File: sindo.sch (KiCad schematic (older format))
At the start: 145 parts

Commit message: Finished lables, might still need pull-downs
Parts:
- removed U?: ESP32-DEVKITC-32D, MODULE_ESP32-DEVKITC-32D, symbol ESP32-DEVKITC-32D:ESP32-DEVKITC-32D
- added J? (x2): Conn_2Rows-13Pins, symbol Connector_Generic:Conn_2Rows-13Pins
- added U?: ESP32DEVKITV1, ESP32-DEVKITV1, symbol ESP32DEVKITV1:ESP32DEVKITV1
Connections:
- net labels added: C10, C11, C6, C7, C8, C9, COL0, COL1, COL10, COL11, COL2, COL3, COL4, COL5, COL6, COL7, COL8, COL9, R0, R1, R2, R3, R4, R5, ROW0, ROW1, ROW2, ROW3, ROW4, ROW5
- wire segments 432 -> 474

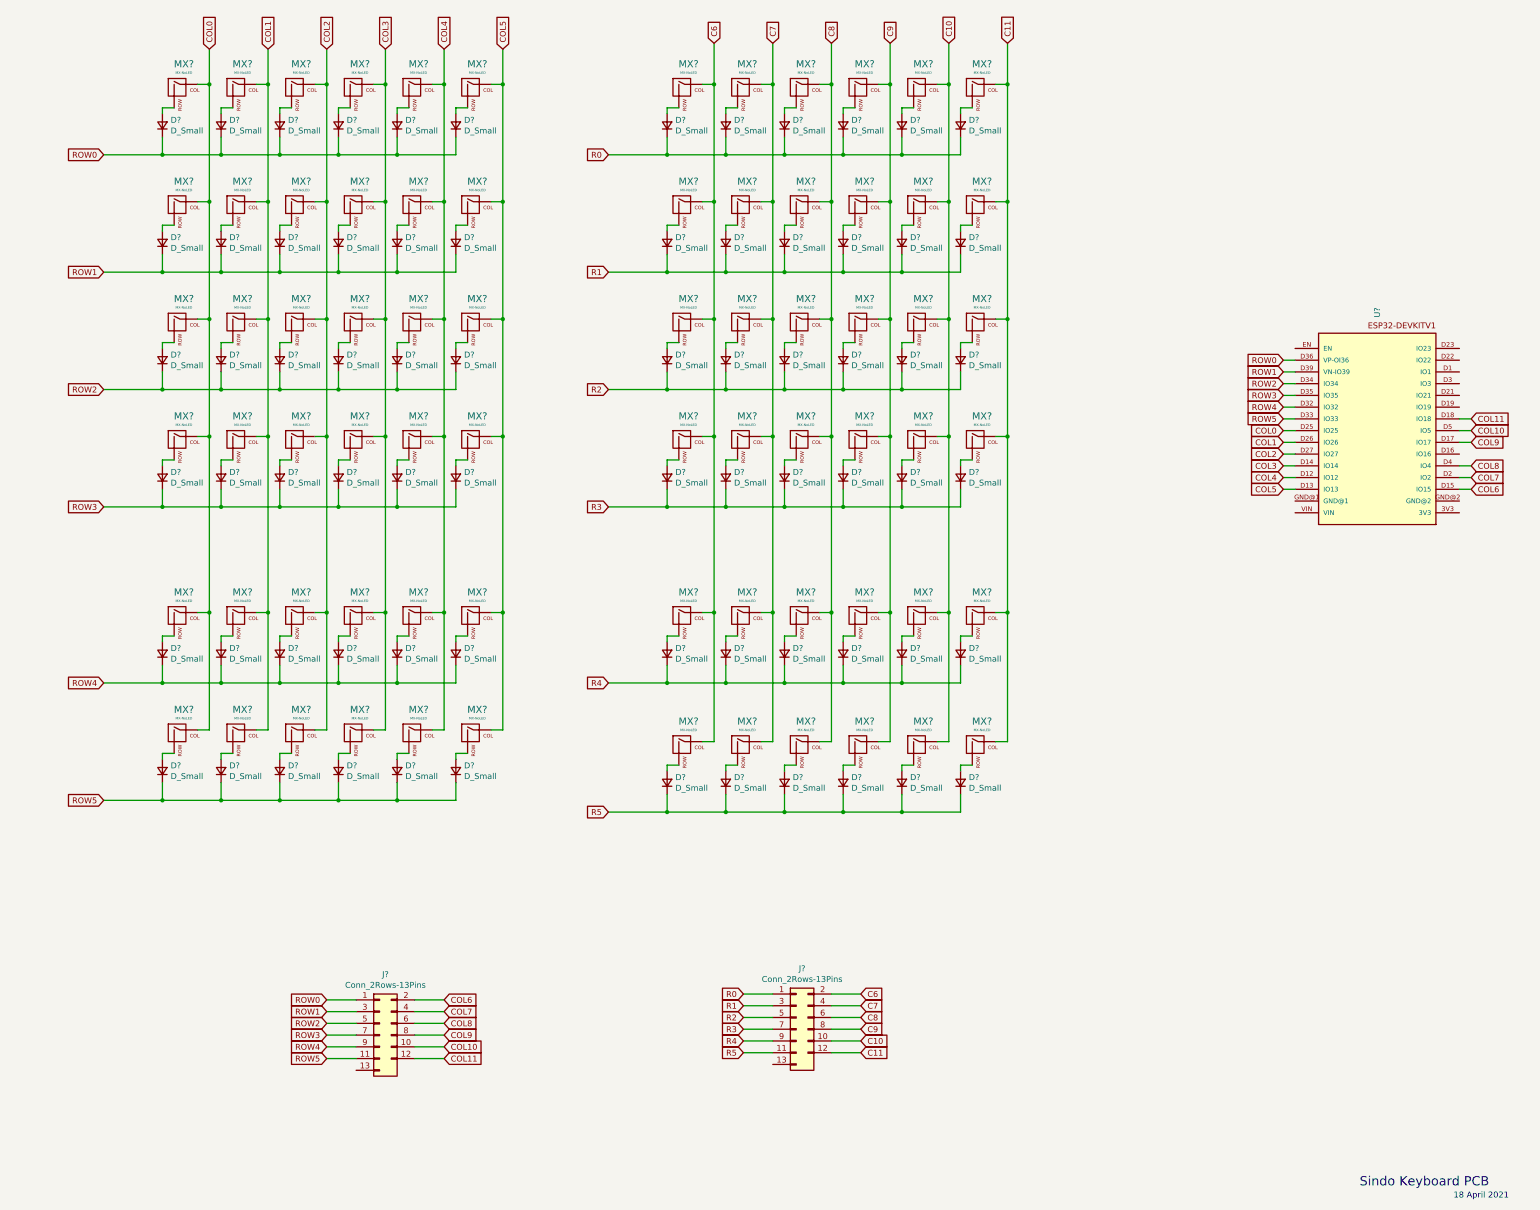
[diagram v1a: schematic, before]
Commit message: Added pull down resistors to rows
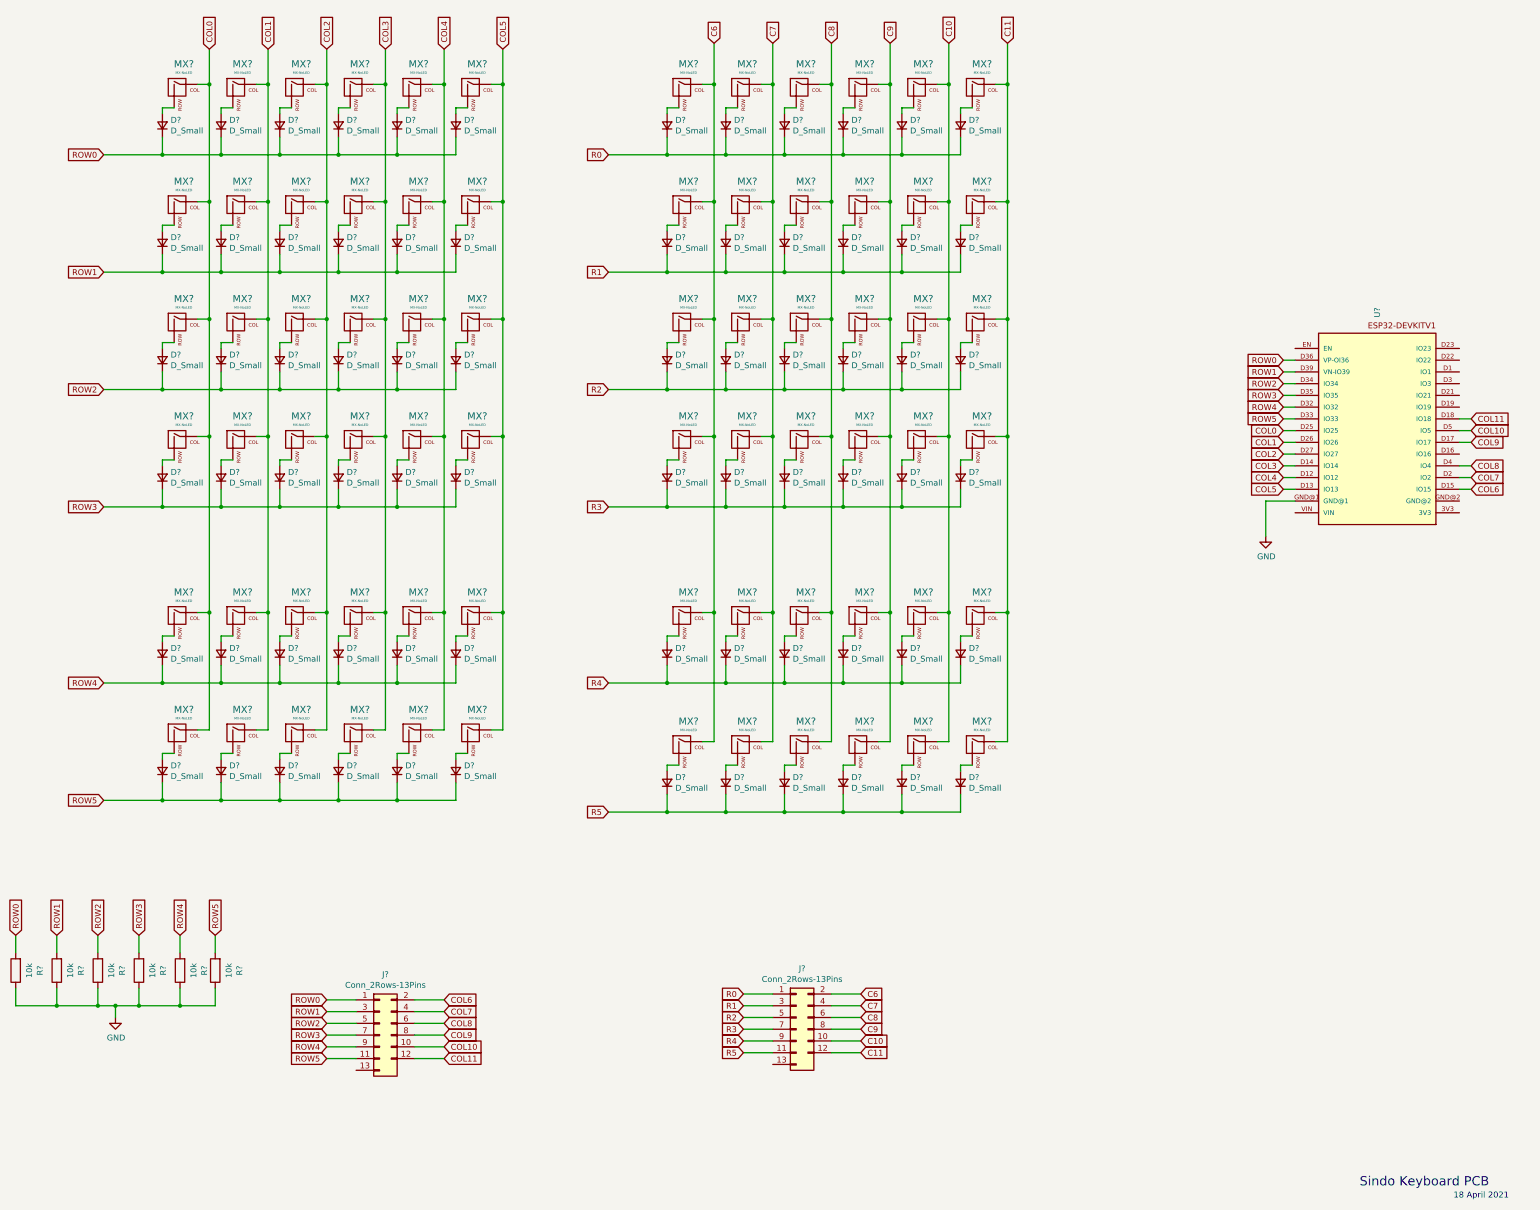
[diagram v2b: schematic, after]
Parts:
- added R? (x6): 10k, symbol Device:R
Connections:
- net ROW0: now also R?.2
- net ROW1: now also R?.2
- net ROW2: now also R?.2
- net ROW3: now also R?.2
- net ROW4: now also R?.2
- net ROW5: now also R?.2
- net GND: now reaches U?.GND@1
- net GND: now also R?.1, R?.1, R?.1, R?.1, R?.1, R?.1
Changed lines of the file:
@@
 Wire Wire Line
 	7950 9300 7700 9300
+Text GLabel 750  8800 1    50   Input ~ 0
+ROW0
+Text GLabel 1100 8800 1    50   Input ~ 0
+ROW1
+Text GLabel 1450 8800 1    50   Input ~ 0
+ROW2
+Text GLabel 1800 8800 1    50   Input ~ 0
+ROW3
+Text GLabel 2150 8800 1    50   Input ~ 0
+ROW4
+Text GLabel 2450 8800 1    50   Input ~ 0
+ROW5
+$Comp
+L power:GND #PWR?
+U 1 1 6084C65C
+P 1600 9500
+F 0 "#PWR?" H 1600 9250 50  0001 C CNN
+F 1 "GND" H 1605 9327 50  0000 C CNN
+F 2 "" H 1600 9500 50  0001 C CNN
+F 3 "" H 1600 9500 50  0001 C CNN
+	1    1600 9500
+	1    0    0    -1
+$EndComp
+$Comp
+L Device:R R?
+U 1 1 60854EEB
+P 750 9100
+F 0 "R?" V 543 9100 50  0000 C CNN
+F 1 "10k" V 634 9100 50  0000 C CNN
+F 2 "" V 680 9100 50  0001 C CNN
+F 3 "~" H 750 9100 50  0001 C CNN
+	1    750  9100
+	-1   0    0    1
+$EndComp
+$Comp
+L Device:R R?
+U 1 1 60856611
+P 1100 9100
+F 0 "R?" V 893 9100 50  0000 C CNN
+F 1 "10k" V 984 9100 50  0000 C CNN
+F 2 "" V 1030 9100 50  0001 C CNN
+F 3 "~" H 1100 9100 50  0001 C CNN
+	1    1100 9100
+	-1   0    0    1
+$EndComp
+$Comp
+L Device:R R?
+U 1 1 6088DADF
+P 1450 9100
+F 0 "R?" V 1243 9100 50  0000 C CNN
+F 1 "10k" V 1334 9100 50  0000 C CNN
+F 2 "" V 1380 9100 50  0001 C CNN
+F 3 "~" H 1450 9100 50  0001 C CNN
+	1    1450 9100
+	-1   0    0    1
+$EndComp
+$Comp
+L Device:R R?
+U 1 1 608C50B4
+P 1800 9100
+F 0 "R?" V 1593 9100 50  0000 C CNN
+F 1 "10k" V 1684 9100 50  0000 C CNN
+F 2 "" V 1730 9100 50  0001 C CNN
+F 3 "~" H 1800 9100 50  0001 C CNN
+	1    1800 9100
+	-1   0    0    1
+$EndComp
+$Comp
+L Device:R R?
+U 1 1 608FC6A0
+P 2150 9100
+F 0 "R?" V 1943 9100 50  0000 C CNN
+F 1 "10k" V 2034 9100 50  0000 C CNN
+F 2 "" V 2080 9100 50  0001 C CNN
+F 3 "~" H 2150 9100 50  0001 C CNN
+	1    2150 9100
+	-1   0    0    1
+$EndComp
+$Comp
+L Device:R R?
+U 1 1 60933B37
+P 2450 9100
+F 0 "R?" V 2243 9100 50  0000 C CNN
+F 1 "10k" V 2334 9100 50  0000 C CNN
+F 2 "" V 2380 9100 50  0001 C CNN
+F 3 "~" H 2450 9100 50  0001 C CNN
+	1    2450 9100
+	-1   0    0    1
+$EndComp
+Wire Wire Line
+	750  8950 750  8800
+Wire Wire Line
+	1100 8800 1100 8950
+Wire Wire Line
+	1450 8950 1450 8800
+Wire Wire Line
+	1800 8800 1800 8950
+Wire Wire Line
+	2150 8950 2150 8800
+Wire Wire Line
+	2450 8800 2450 8950
+Wire Wire Line
+	750  9250 750  9400
+Wire Wire Line
+	750  9400 1100 9400
+Wire Wire Line
+	1600 9400 1600 9500
+Wire Wire Line
+	1100 9250 1100 9400
+Connection ~ 1100 9400
+Wire Wire Line
+	1100 9400 1450 9400
+Wire Wire Line
+	1450 9250 1450 9400
+Connection ~ 1450 9400
+Wire Wire Line
+	1450 9400 1600 9400
+Wire Wire Line
+	2450 9250 2450 9400
+Wire Wire Line
+	2450 9400 2150 9400
+Connection ~ 1600 9400
+Wire Wire Line
+	1800 9250 1800 9400
+Connection ~ 1800 9400
+Wire Wire Line
+	1800 9400 1600 9400
+Wire Wire Line
+	2150 9250 2150 9400
+Connection ~ 2150 9400
+Wire Wire Line
+	2150 9400 1800 9400
+$Comp
+L power:GND #PWR?
+U 1 1 60E4395C
+P 11400 5400
+F 0 "#PWR?" H 11400 5150 50  0001 C CNN
+F 1 "GND" H 11405 5227 50  0000 C CNN
+F 2 "" H 11400 5400 50  0001 C CNN
+F 3 "" H 11400 5400 50  0001 C CNN
+	1    11400 5400
+	1    0    0    -1
+$EndComp
+Wire Wire Line
+	11650 5100 11400 5100
+Wire Wire Line
+	11400 5100 11400 5400
 $EndSCHEMATC

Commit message: Used a better header, linked schematic to footprints.
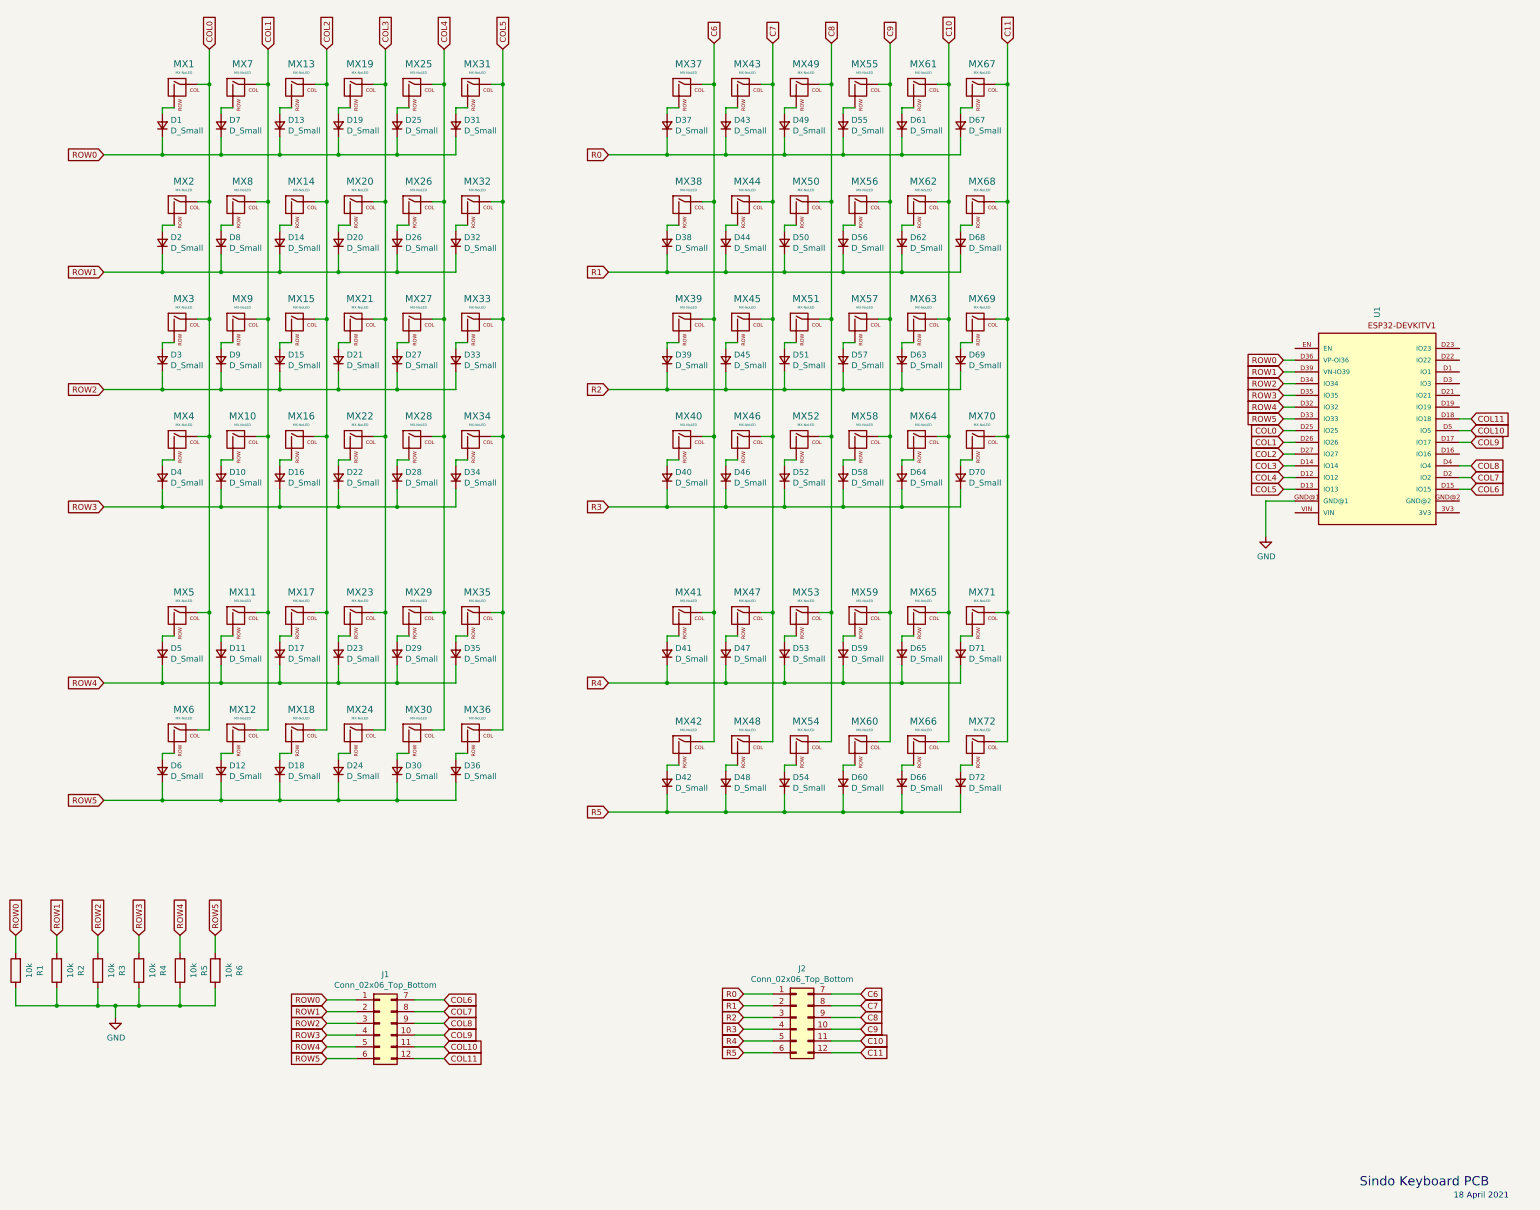
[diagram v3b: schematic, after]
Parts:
- removed J? (x2): Conn_2Rows-13Pins, symbol Connector_Generic:Conn_2Rows-13Pins
- added J1, J2: Conn_02x06_Top_Bottom, Connector_PinHeader_1.27mm:PinHeader_2x06_P1.27mm_Vertical, symbol Connector_Generic:Conn_02x06_Top_Bottom
- D1, D10, D11, D12, D13, D14, D15, D16, D17, D18, D19, D2, D20, D21, D22, D23, D24, D25, D26, D27, D28, D29, D3, D30, D31, D32, D33, D34, D35, D36, D37, D38, D39, D4, D40, D41, D42, D43, D44, D45, D46, D47, D48, D49, D5, D50, D51, D52, D53, D54, D55, D56, D57, D58, D59, D6, D60, D61, D62, D63, D64, D65, D66, D67, D68, D69, D7, D70, D71, D72, D8, D9: renamed from D?; footprint (none) -> Diode_THT:D_DO-35_SOD27_P3.81mm_Vertical_AnodeUp
- MX1, MX10, MX11, MX12, MX13, MX14, MX15, MX16, MX17, MX18, MX19, MX2, MX20, MX21, MX22, MX23, MX24, MX25, MX26, MX27, MX28, MX29, MX3, MX30, MX31, MX32, MX33, MX34, MX35, MX36, MX37, MX38, MX39, MX4, MX40, MX41, MX42, MX43, MX44, MX45, MX46, MX47, MX48, MX49, MX5, MX50, MX51, MX52, MX53, MX54, MX55, MX56, MX57, MX58, MX59, MX6, MX60, MX61, MX62, MX63, MX64, MX65, MX66, MX67, MX68, MX69, MX7, MX70, MX71, MX72, MX8, MX9: renamed from MX?; footprint (none) -> MX_Only:MXOnly-1U-NoLED
- R1, R2, R3, R4, R5, R6: renamed from R?; footprint (none) -> Resistor_THT:R_Axial_DIN0207_L6.3mm_D2.5mm_P5.08mm_Vertical
- U1: renamed from U?; footprint ESP32-DEVKITV1 -> ESP32DEVKITV1:ESP32-DEVKITV1
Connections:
- net C10: now also J2.11 (Pin_11)
- net C11: now also J2.12 (Pin_12)
- net C6: now also J2.7 (Pin_7)
- net C7: now also J2.8 (Pin_8)
- net C8: now also J2.9 (Pin_9)
- net C9: now also J2.10 (Pin_10)
- net COL10: now also J1.11 (Pin_11)
- net COL11: now also J1.12 (Pin_12)
- net COL6: now also J1.7 (Pin_7)
- net COL7: now also J1.8 (Pin_8)
- net COL8: now also J1.9 (Pin_9)
- net COL9: now also J1.10 (Pin_10)
- net R0: now also J2.1 (Pin_1)
- net R1: now also J2.2 (Pin_2)
- net R2: now also J2.3 (Pin_3)
- net R3: now also J2.4 (Pin_4)
- net R4: now also J2.5 (Pin_5)
- net R5: now also J2.6 (Pin_6)
- net ROW0: now also J1.1 (Pin_1)
- net ROW1: now also J1.2 (Pin_2)
- net ROW2: now also J1.3 (Pin_3)
- net ROW3: now also J1.4 (Pin_4)
- net ROW4: now also J1.5 (Pin_5)
- net ROW5: now also J1.6 (Pin_6)

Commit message: Started with the first half layout
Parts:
- D1, D10, D11, D12, D13, D14, D15, D16, D17, D18, D19, D2, D20, D21, D22, D23, D24, D25, D26, D27, D28, D29, D3, D30, D31, D32, D33, D34, D35, D36, D37, D38, D39, D4, D40, D41, D42, D43, D44, D45, D46, D47, D48, D49, D5, D50, D51, D52, D53, D54, D55, D56, D57, D58, D59, D6, D60, D61, D62, D63, D64, D65, D66, D67, D68, D69, D7, D70, D71, D72, D8, D9: footprint Diode_THT:D_DO-35_SOD27_P3.81mm_Vertical_AnodeUp -> Diode_THT:D_DO-35_SOD27_P7.62mm_Horizontal

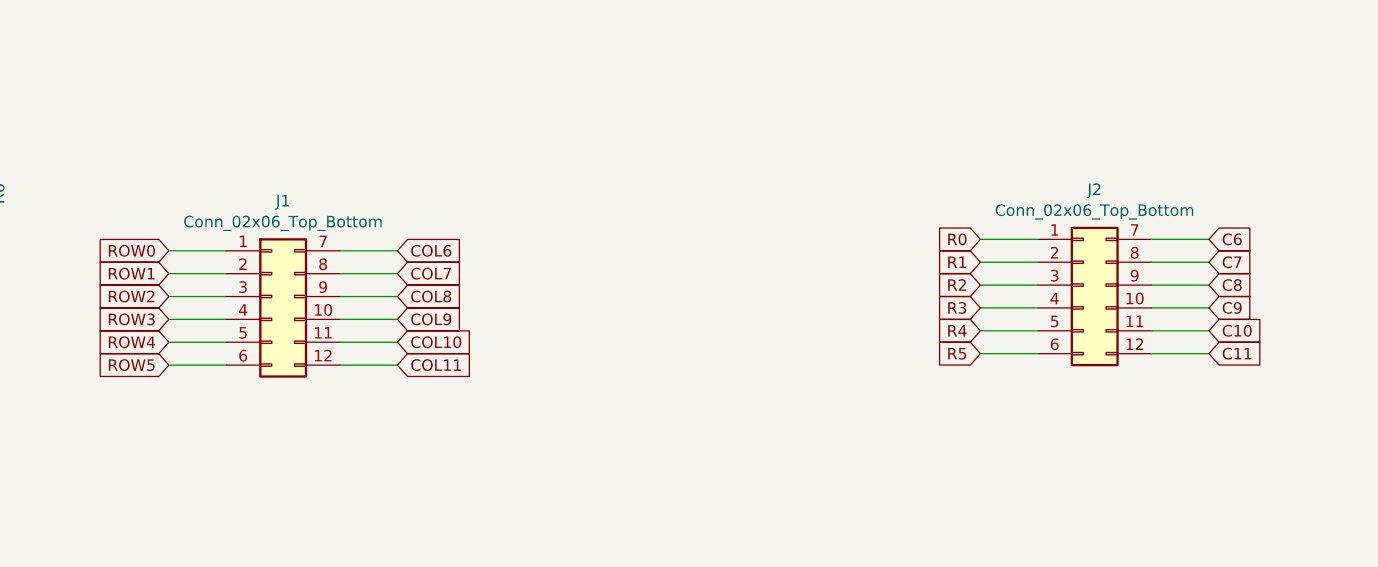
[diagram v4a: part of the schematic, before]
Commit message: Using a better header footprint.
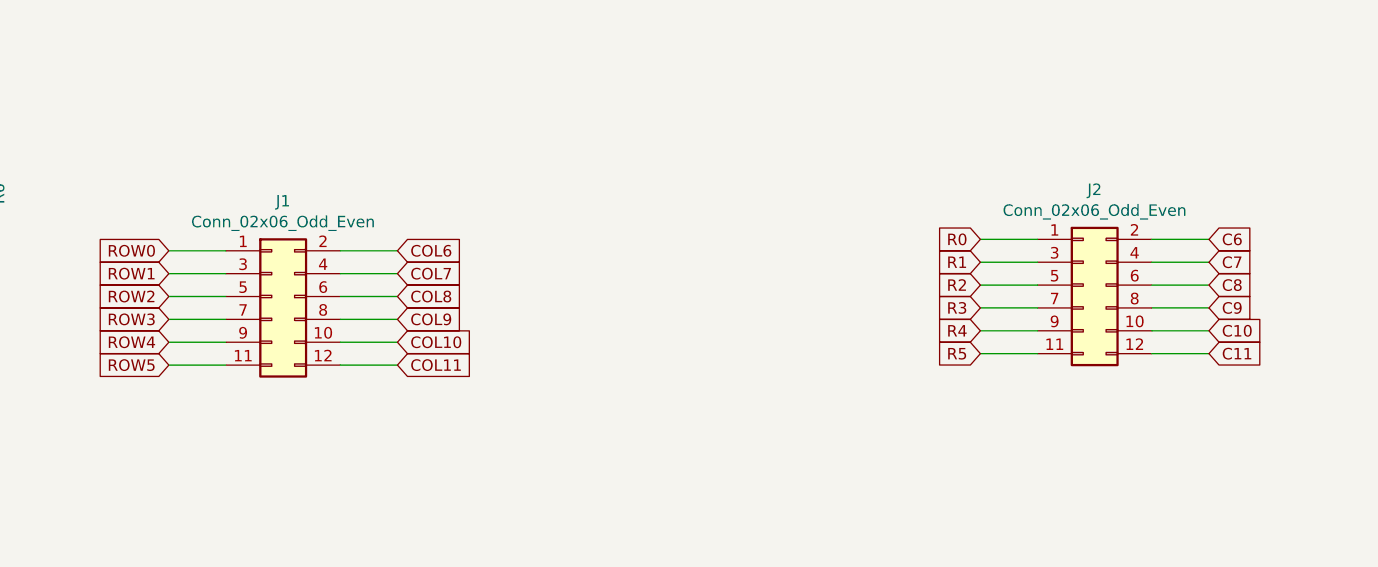
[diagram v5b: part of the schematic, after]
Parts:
- removed J1, J2: Conn_02x06_Top_Bottom, Connector_PinHeader_1.27mm:PinHeader_2x06_P1.27mm_Vertical, symbol Connector_Generic:Conn_02x06_Top_Bottom
- added J1, J2: Conn_02x06_Odd_Even, Connector_PinHeader_1.27mm:PinHeader_2x06_P1.27mm_Vertical, symbol Connector_Generic:Conn_02x06_Odd_Even
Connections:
- net C10: now also J2.10 (Pin_10)
- net C11: now also J2.12 (Pin_12)
- net C6: now also J2.2 (Pin_2)
- net C7: now also J2.4 (Pin_4)
- net C8: now also J2.6 (Pin_6)
- net C9: now also J2.8 (Pin_8)
- net COL10: now also J1.10 (Pin_10)
- net COL11: now also J1.12 (Pin_12)
- net COL6: now also J1.2 (Pin_2)
- net COL7: now also J1.4 (Pin_4)
- net COL8: now also J1.6 (Pin_6)
- net COL9: now also J1.8 (Pin_8)
- net R0: now also J2.1 (Pin_1)
- net R1: now also J2.3 (Pin_3)
- net R2: now also J2.5 (Pin_5)
- net R3: now also J2.7 (Pin_7)
- net R4: now also J2.9 (Pin_9)
- net R5: now also J2.11 (Pin_11)
- net ROW0: now also J1.1 (Pin_1)
- net ROW1: now also J1.3 (Pin_3)
- net ROW2: now also J1.5 (Pin_5)
- net ROW3: now also J1.7 (Pin_7)
- net ROW4: now also J1.9 (Pin_9)
- net ROW5: now also J1.11 (Pin_11)
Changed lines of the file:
@@
 	11400 5100 11400 5400
 $Comp
-L Connector_Generic:Conn_02x06_Top_Bottom J1
-U 1 1 60EF8272
+L Connector_Generic:Conn_02x06_Odd_Even J1
+U 1 1 60987DB5
 P 3850 9550
 F 0 "J1" H 3900 9967 50  0000 C CNN
-F 1 "Conn_02x06_Top_Bottom" H 3900 9876 50  0000 C CNN
+F 1 "Conn_02x06_Odd_Even" H 3900 9876 50  0000 C CNN
 F 2 "Connector_PinHeader_1.27mm:PinHeader_2x06_P1.27mm_Vertical" H 3850 9550 50  0001 C CNN
 F 3 "~" H 3850 9550 50  0001 C CNN
@@
 $EndComp
 $Comp
-L Connector_Generic:Conn_02x06_Top_Bottom J2
-U 1 1 60FC0EF5
+L Connector_Generic:Conn_02x06_Odd_Even J2
+U 1 1 60A0B7A7
 P 7400 9500
 F 0 "J2" H 7450 9917 50  0000 C CNN
-F 1 "Conn_02x06_Top_Bottom" H 7450 9826 50  0000 C CNN
+F 1 "Conn_02x06_Odd_Even" H 7450 9826 50  0000 C CNN
 F 2 "Connector_PinHeader_1.27mm:PinHeader_2x06_P1.27mm_Vertical" H 7400 9500 50  0001 C CNN
 F 3 "~" H 7400 9500 50  0001 C CNN
